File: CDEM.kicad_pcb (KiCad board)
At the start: 2 copper layers, 80.7 x 51.5 mm, 43 parts, among them J1 USB_C_Receptacle_USB2.0, J2 6P6C, J3 Conn_01x04, J4 Conn_01x03, Q1 2N7002, Q2 S8050, Q3 S8050, SW1 BTN, SW2 RESET, U1 MCP1825S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

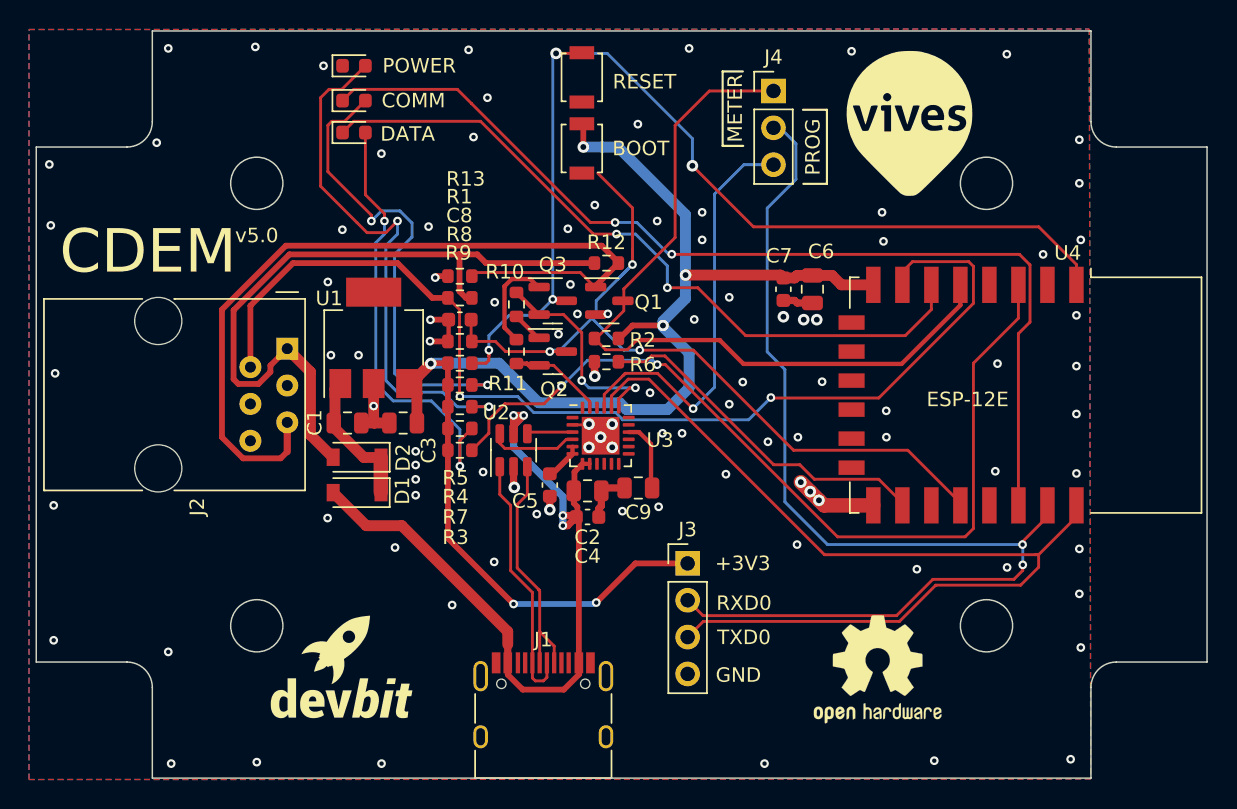
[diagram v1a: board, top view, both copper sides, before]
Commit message: fix unconnected trace to boot button
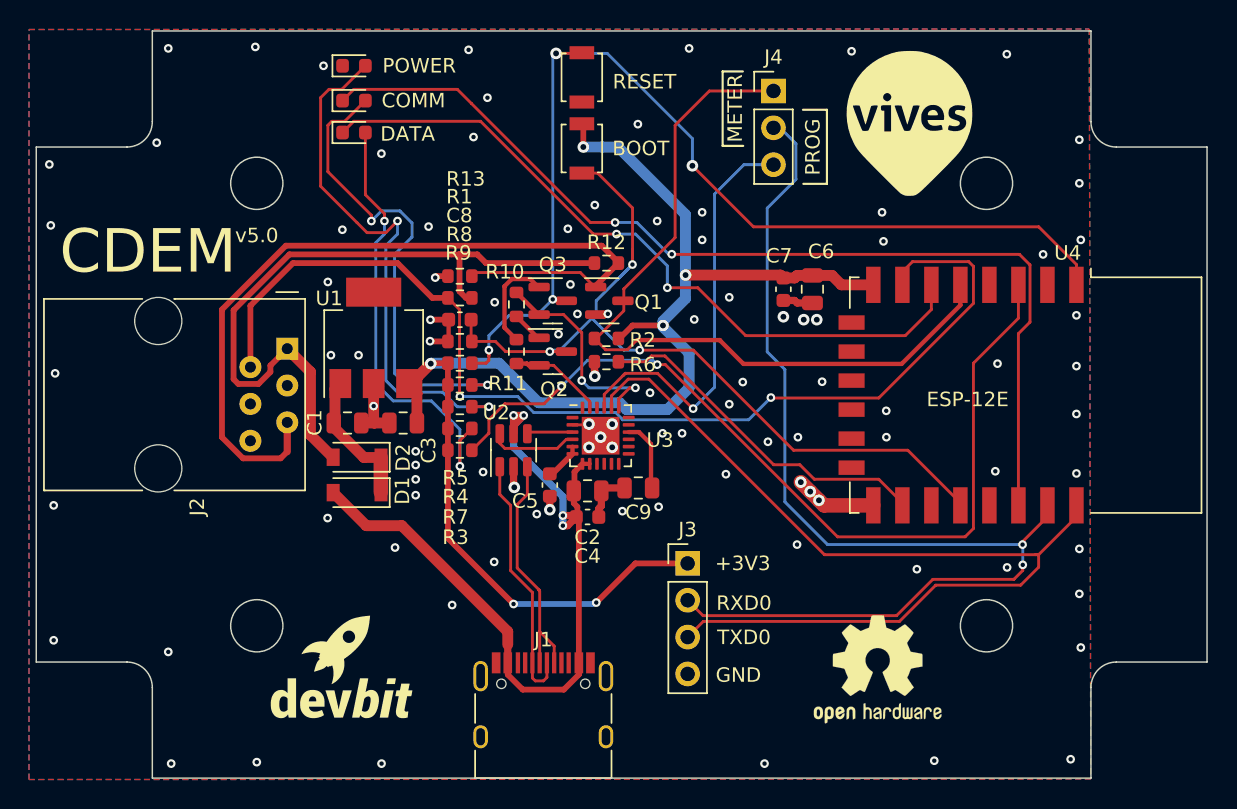
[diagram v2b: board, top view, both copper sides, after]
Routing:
- net /GPIO0: track 57.1 -> 58.2 mm
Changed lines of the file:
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@@
-(kicad_pcb (version 20210722) (generator pcbnew)
+(kicad_pcb (version 20211014) (generator pcbnew)
   (general
     (thickness 1.6)
@@
   (gr_circle (center 41.6 91.2) (end 43.4 91.2) (layer "Edge.Cuts") (width 0.1) (fill none))
   (gr_circle (center 41.6 121.7) (end 43.4 121.7) (layer "Edge.Cuts") (width 0.1) (fill none))
-  (gr_arc (start 32.65 125.95) (end 34.4 125.95) (angle -90) (layer "Edge.Cuts") (width 0.1))
+  (gr_arc (start 32.65 124.2) (mid 33.887437 124.712563) (end 34.4 125.95) (layer "Edge.Cuts") (width 0.1))
   (gr_line (start 99.1 132.2) (end 34.4 132.2) (layer "Edge.Cuts") (width 0.1))
   (gr_line (start 107.1 88.7) (end 107.1 124.2) (layer "Edge.Cuts") (width 0.1))
   (gr_line (start 34.4 132.2) (end 34.4 125.95) (layer "Edge.Cuts") (width 0.1))
-  (gr_arc (start 100.85 125.95) (end 100.85 124.2) (angle -90) (layer "Edge.Cuts") (width 0.1))
+  (gr_arc (start 99.1 125.95) (mid 99.612563 124.712563) (end 100.85 124.2) (layer "Edge.Cuts") (width 0.1))
   (gr_line (start 99.1 80.7) (end 99.1 86.95) (layer "Edge.Cuts") (width 0.1))
   (gr_line (start 26.4 88.7) (end 32.65 88.7) (layer "Edge.Cuts") (width 0.1))
   (gr_line (start 34.4 86.95) (end 34.4 80.7) (layer "Edge.Cuts") (width 0.1))
-  (gr_arc (start 100.85 86.95) (end 99.1 86.95) (angle -90) (layer "Edge.Cuts") (width 0.1))
+  (gr_arc (start 100.85 88.7) (mid 99.612563 88.187437) (end 99.1 86.95) (layer "Edge.Cuts") (width 0.1))
   (gr_line (start 34.4 80.7) (end 99.1 80.7) (layer "Edge.Cuts") (width 0.1))
-  (gr_arc (start 32.65 86.95) (end 32.65 88.7) (angle -90) (layer "Edge.Cuts") (width 0.1))
+  (gr_arc (start 34.4 86.95) (mid 33.887437 88.187437) (end 32.65 88.7) (layer "Edge.Cuts") (width 0.1))
   (gr_circle (center 91.9 91.2) (end 93.7 91.2) (layer "Edge.Cuts") (width 0.1) (fill none))
   (gr_line (start 100.85 88.7) (end 107.1 88.7) (layer "Edge.Cuts") (width 0.1))
@@
     (pts (xy 34.4 80.7) (xy 99.1 80.7))
     (height -3.6)
-    (gr_text "64,7000 mm" (at 66.75 75.95) (layer "User.8")
+    (gr_text "64.7000 mm" (at 66.75 75.95) (layer "User.8")
       (effects (font (size 1 1) (thickness 0.15)))
     )
@@
     (pts (xy 26.4 88.7) (xy 26.4 124.2))
     (height 3)
-    (gr_text "35,5000 mm" (at 22.25 106.45 90) (layer "User.8")
+    (gr_text "35.5000 mm" (at 22.25 106.45 90) (layer "User.8")
       (effects (font (size 1 1) (thickness 0.15)))
     )
@@
     (pts (xy 26.4 80.7) (xy 26.4 132.2))
     (height 7.499999)
-    (gr_text "51,5000 mm" (at 17.750001 106.45 90) (layer "User.8")
+    (gr_text "51.5000 mm" (at 17.750001 106.45 90) (layer "User.8")
       (effects (font (size 1 1) (thickness 0.15)))
     )
@@
     (pts (xy 26.4 80.7) (xy 107.1 80.7))
     (height -5.8)
-    (gr_text "80,7000 mm" (at 66.75 73.75) (layer "User.8")
+    (gr_text "80.7000 mm" (at 66.75 73.75) (layer "User.8")
       (effects (font (size 1 1) (thickness 0.15)))
     )
@@
     (pts (xy 107.1 91.2) (xy 107.1 121.7))
     (height -4.5)
-    (gr_text "30,5000 mm" (at 110.45 106.45 90) (layer "User.9")
+    (gr_text "30.5000 mm" (at 110.45 106.45 90) (layer "User.9")
       (effects (font (size 1 1) (thickness 0.15)))
     )
@@
     (pts (xy 107.1 132.2) (xy 107.1 121.7))
     (height 4.5)
-    (gr_text "10,5000 mm" (at 110.45 126.95 90) (layer "User.9")
+    (gr_text "10.5000 mm" (at 110.45 126.95 90) (layer "User.9")
       (effects (font (size 1 1) (thickness 0.15)))
     )
@@
     (pts (xy 17.7222 115.1942) (xy 17.7222 130.3942))
     (height -4.5)
-    (gr_text "15,2000 mm" (at 21.0722 122.7942 90) (layer "User.9")
+    (gr_text "15.2000 mm" (at 21.0722 122.7942 90) (layer "User.9")
       (effects (font (size 1 1) (thickness 0.15)))
     )
@@
     (pts (xy 107.1 132.2) (xy 91.9 132.2))
     (height -4.5)
-    (gr_text "15,2000 mm" (at 99.5 135.55) (layer "User.9")
+    (gr_text "15.2000 mm" (at 99.5 135.55) (layer "User.9")
       (effects (font (size 1 1) (thickness 0.15)))
     )
@@
     (pts (xy 107.1 91.2) (xy 107.1 80.7))
     (height 4.5)
-    (gr_text "10,5000 mm" (at 110.45 85.95 90) (layer "User.9")
+    (gr_text "10.5000 mm" (at 110.45 85.95 90) (layer "User.9")
       (effects (font (size 1 1) (thickness 0.15)))
     )
@@
     (pts (xy 17.7222 115.1942) (xy 17.7222 64.8942))
     (height 4.5)
-    (gr_text "50,3000 mm" (at 21.0722 90.0442 90) (layer "User.9")
+    (gr_text "50.3000 mm" (at 21.0722 90.0442 90) (layer "User.9")
       (effects (font (size 1 1) (thickness 0.15)))
     )
@@
   (segment (start 90.1 113.4) (end 90.1 113.22572) (width 0.2) (layer "F.Cu") (net 4))
   (segment (start 71.697082 102.7) (end 68 102.7) (width 0.2) (layer "F.Cu") (net 4))
+  (segment (start 65.098 90.498) (end 64.008 90.498) (width 0.2) (layer "F.Cu") (net 4))
+  (segment (start 67.5 92.9) (end 65.098 90.498) (width 0.2) (layer "F.Cu") (net 4))
   (segment (start 67.5 96.291472) (end 67.495736 96.295736) (width 0.2) (layer "F.Cu") (net 4))
   (segment (start 58.05 102.1) (end 56.425 102.1) (width 0.2) (layer "F.Cu") (net 4))
   (segment (start 61.8 102.8) (end 58.75 102.8) (width 0.2) (layer "F.Cu") (net 4))
-  (segment (start 67.5 92.9) (end 67.5 95.8) (width 0.2) (layer "F.Cu") (net 4))
   (segment (start 58.75 102.8) (end 58.05 102.1) (width 0.2) (layer "F.Cu") (net 4))
   (segment (start 56.375 100.6) (end 56.375 102.05) (width 0.2) (layer "F.Cu") (net 4))
   (segment (start 56.375 102.05) (end 56.425 102.1) (width 0.2) (layer "F.Cu") (net 4))
+  (segment (start 67.5 95.8) (end 67.5 92.9) (width 0.2) (layer "F.Cu") (net 4))
   (segment (start 67.495736 95.804264) (end 67.5 95.8) (width 0.2) (layer "F.Cu") (net 4))
   (segment (start 86.47429 109.60001) (end 78.597092 109.60001) (width 0.2) (layer "F.Cu") (net 4))
@@
   (segment (start 67.495736 96.8) (end 67.495736 95.804264) (width 0.2) (layer "F.Cu") (net 4))
   (segment (start 78.597092 109.60001) (end 71.697082 102.7) (width 0.2) (layer "F.Cu") (net 4))
-  (segment (start 65.1 90.5) (end 67.5 92.9) (width 0.2) (layer "F.Cu") (net 4))
   (via (at 67.495736 96.8) (size 0.6) (drill 0.3) (layers "F.Cu" "B.Cu") (net 4))
   (via (at 61.8 102.8) (size 0.6) (drill 0.3) (layers "F.Cu" "B.Cu") (net 4))
